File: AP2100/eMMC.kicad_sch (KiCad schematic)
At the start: 33 parts, among them U21 EMMC04G-M627-A01, U7 LS1043ASE7xxx

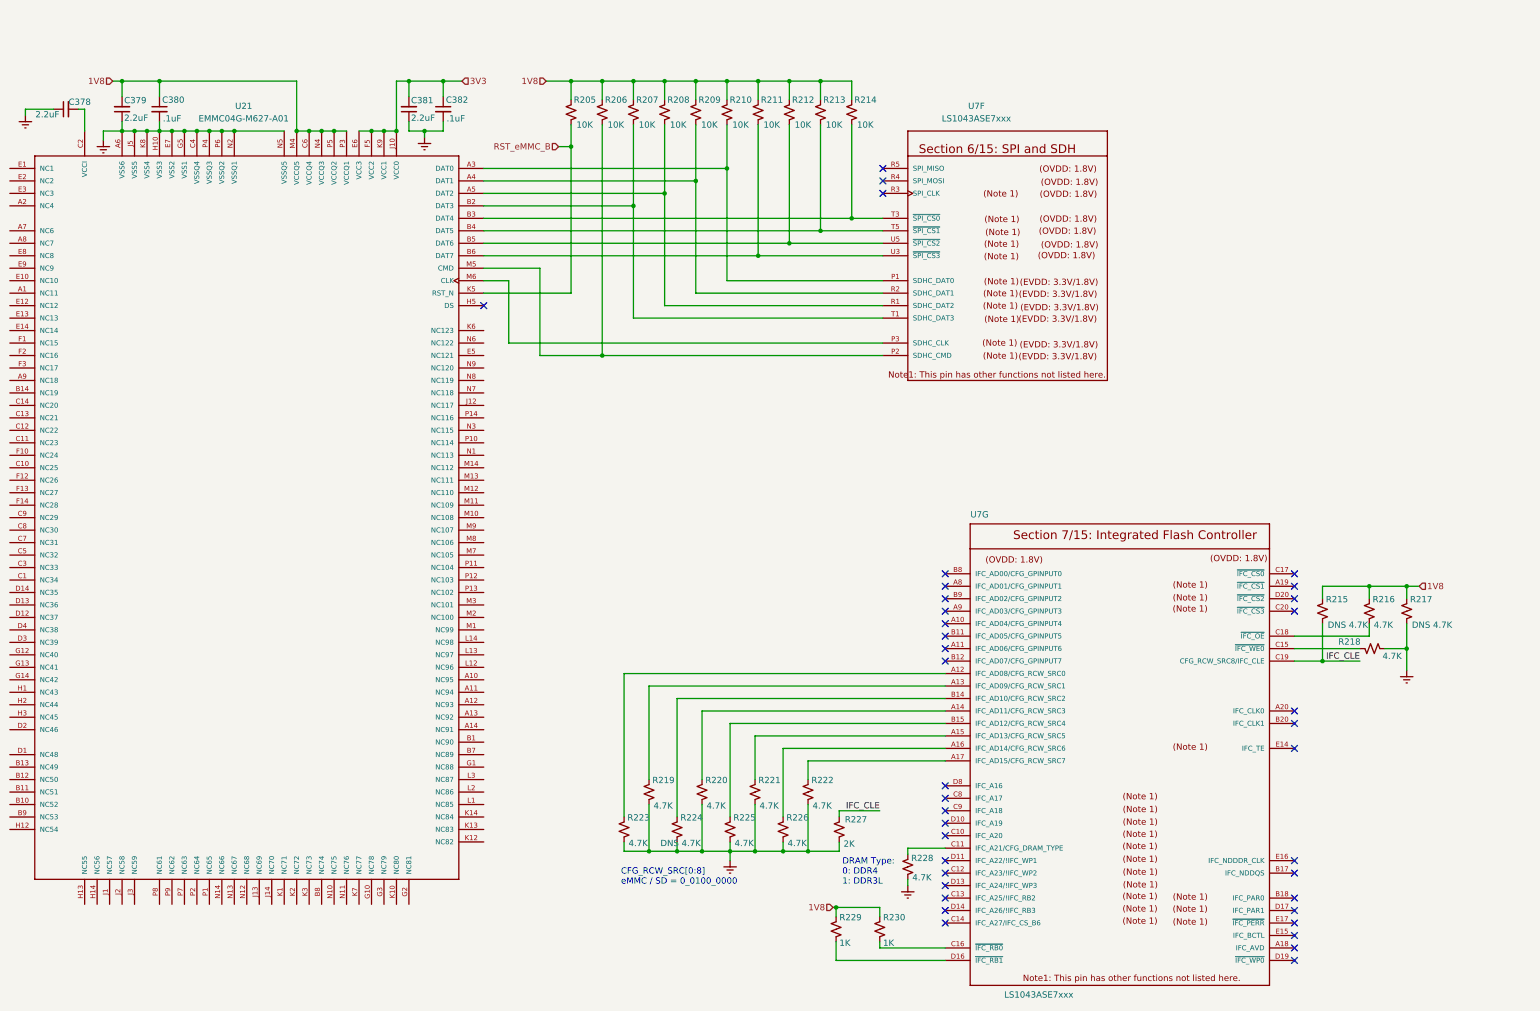
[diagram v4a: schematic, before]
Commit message: More cleanups - fix incorrect serial console pinout Add netclasses
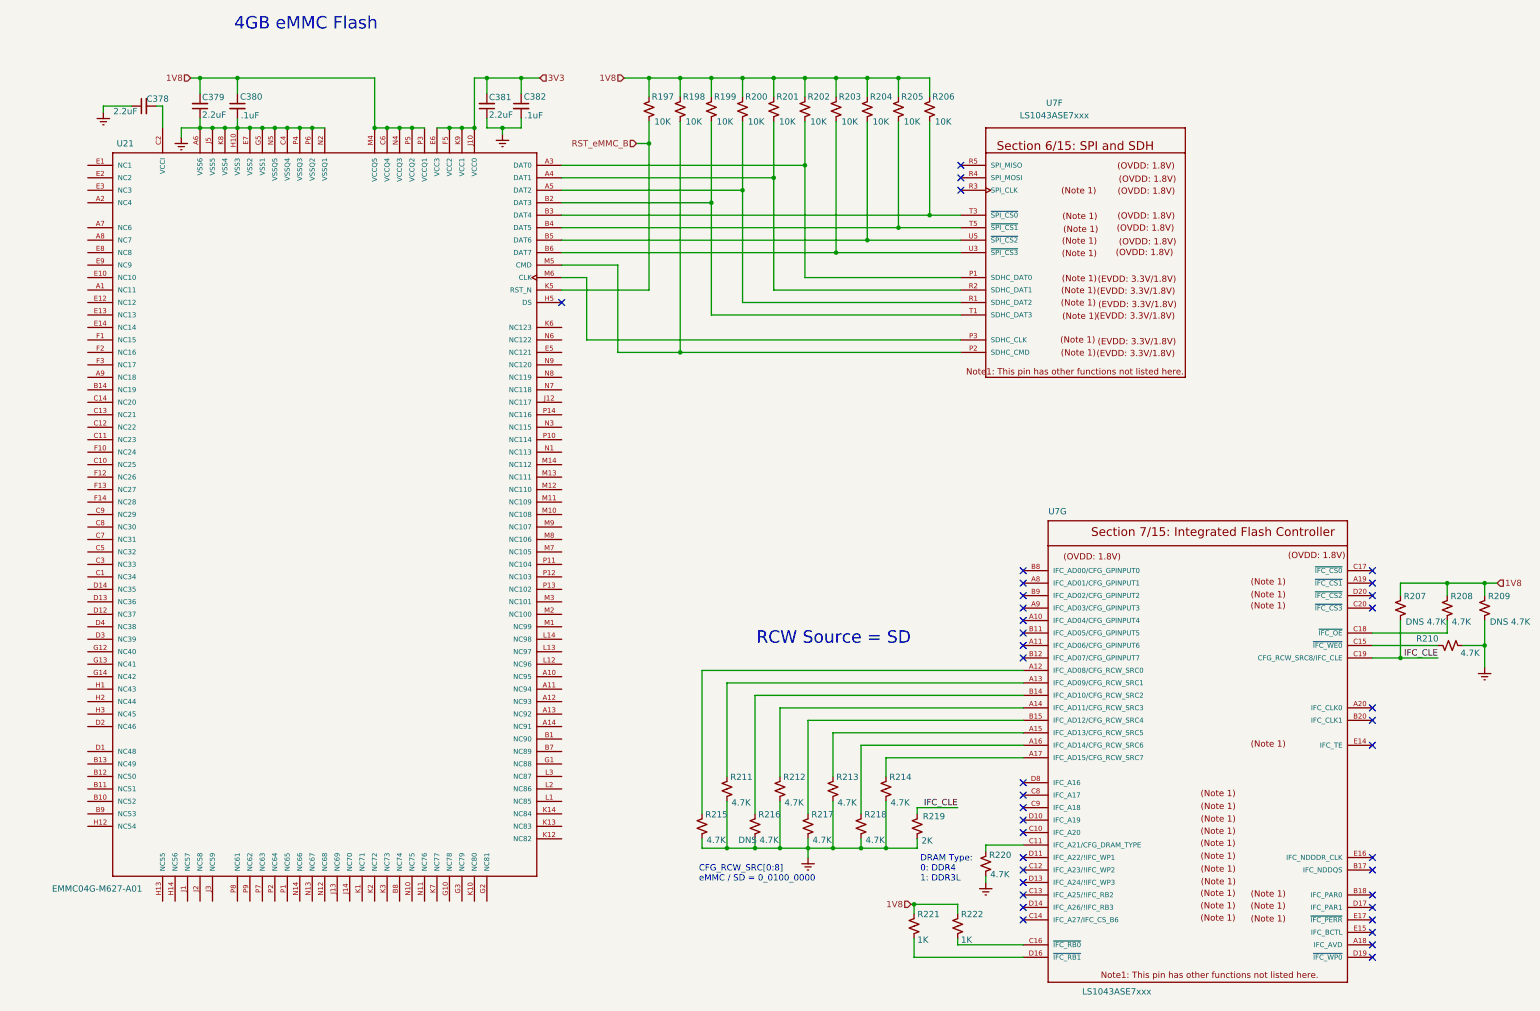
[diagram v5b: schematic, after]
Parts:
- U21: PartsBoxID EMMC04G-M627-A01 -> EMMC-4GB-WFBGA153
- renumbered R205 to R197, R206 to R198, R207 to R199, R208 to R200, R209 to R201, R210 to R202, R211 to R203, R212 to R204, R213 to R205, R214 to R206, R215 to R207, R216 to R208, R217 to R209, R218 to R210, R219 to R211, R220 to R212, R221 to R213, R222 to R214, R223 to R215, R224 to R216, R225 to R217, R226 to R218, R227 to R219, R228 to R220, R229 to R221, R230 to R222
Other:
- note added: "4GB eMMC Flash"
- note added: "RCW Source = SD"
- company: (none) -> ISis ImageStream Internet Solutions, Inc.
- title: (none) -> AP2100
- moved on the sheet: C378, C379, C380, C381, C382, R197, R198, R199, R200, R201, R202, R203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
